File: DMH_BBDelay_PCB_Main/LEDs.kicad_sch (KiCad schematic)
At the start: 7 parts, among them SW2 SW_DPDT_x2

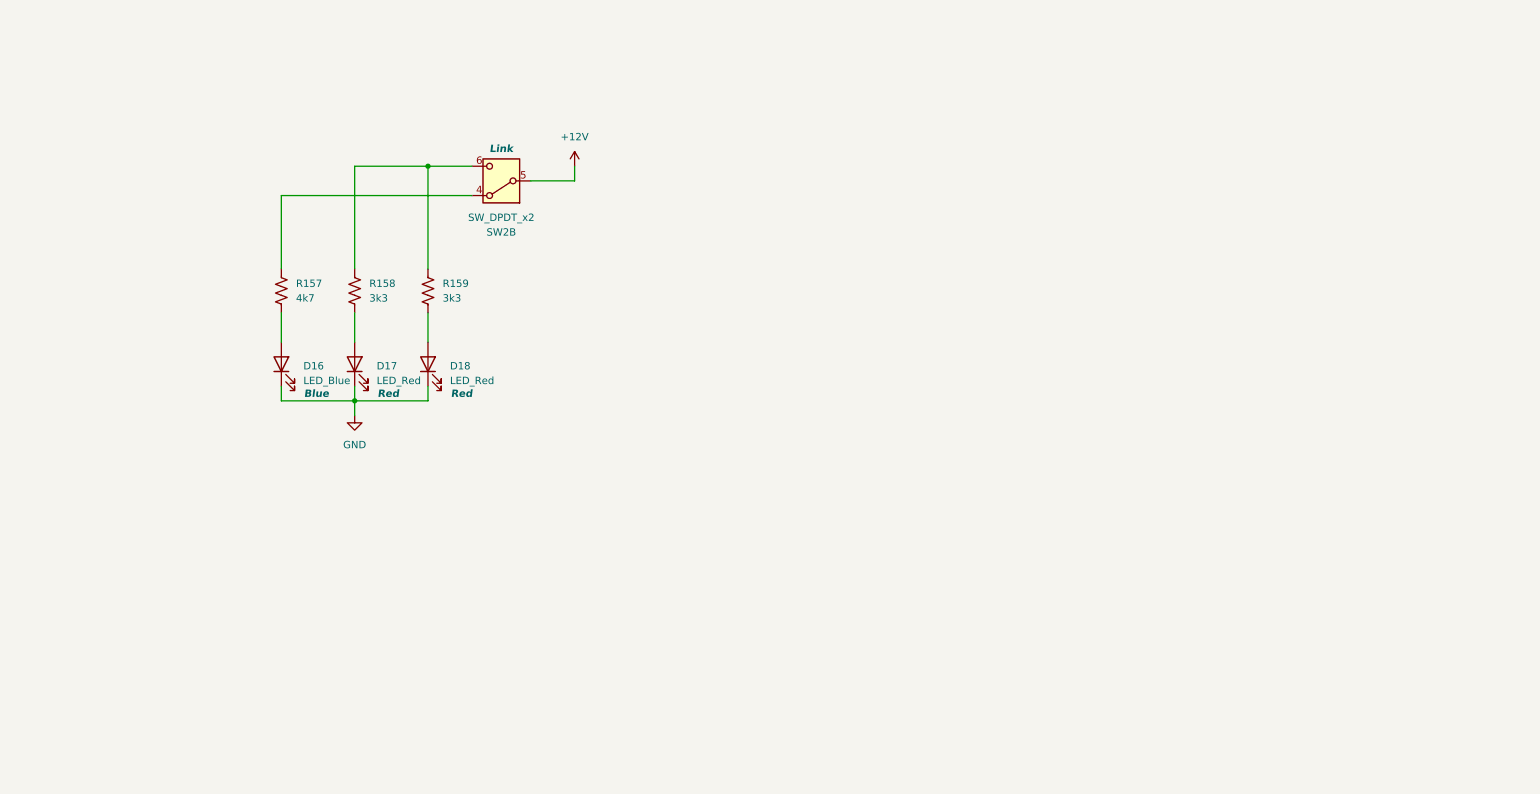
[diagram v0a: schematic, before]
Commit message: Added clock dividers for LEDs
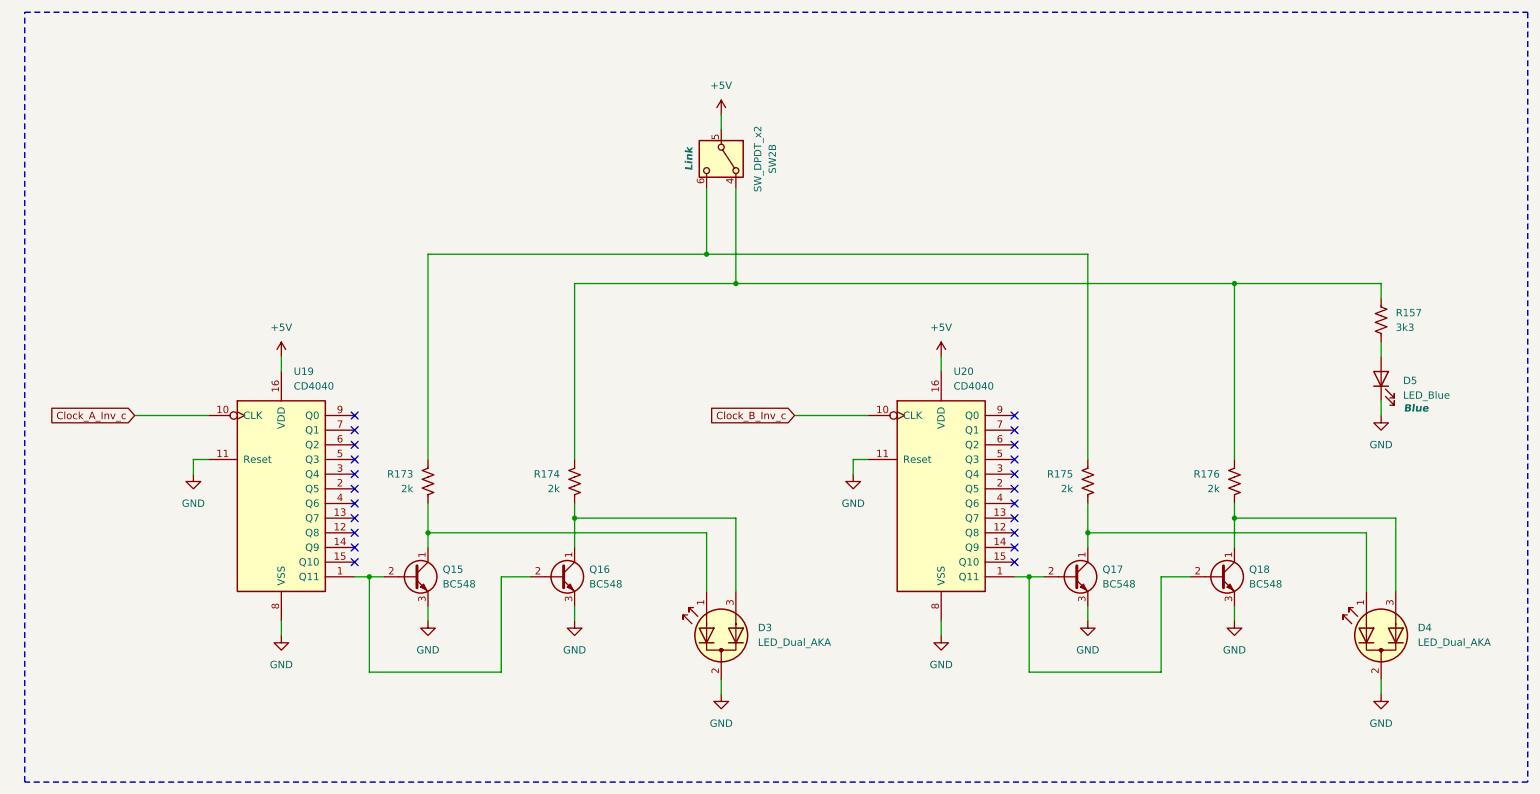
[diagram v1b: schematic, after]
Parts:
- removed D16: LED_Blue, LED_THT:LED_D3.0mm, symbol Device:LED
- removed D17, D18: LED_Red, LED_THT:LED_D3.0mm, symbol Device:LED
- removed R158, R159: 3k3, Resistor_THT:R_Axial_DIN0207_L6.3mm_D2.5mm_P7.62mm_Horizontal, symbol Device:R_US
- added D3, D4: LED_Dual_AKA, SynthStuff:LED_D3.0mm-2color, symbol Device:LED_Dual_AKA
- added D5: LED_Blue, LED_THT:LED_D3.0mm, symbol Device:LED
- added Q15, Q16, Q17, Q18: BC548, Package_TO_SOT_THT:TO-92L_Inline_Wide, symbol Transistor_BJT:BC548
- added R173, R174, R175, R176: 2k, Resistor_THT:R_Axial_DIN0207_L6.3mm_D2.5mm_P7.62mm_Horizontal, symbol Device:R_US
- added U19, U20: CD4040, Package_DIP:DIP-16_W7.62mm_Socket, symbol 4xxx:4040
- R157: value 4k7 -> 3k3
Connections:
- net GND: now also D3.2 (K), D4.2 (K), D5.1 (K), Q15.3 (E), Q16.3 (E), Q17.3 (E), Q18.3 (E), U19.11 (Reset), U19.8 (VSS), U20.11 (Reset), U20.8 (VSS)
- net at R157.2: now also D5.2 (A)
- net at SW2.6 (C): now also R173.2, R175.2
- net at R157.1, SW2.4 (A): now also R174.2, R176.2
- net +12V renamed +5V
- net +5V: now also U19.16 (VDD), U20.16 (VDD)
- new net: D3.1 (A1), Q15.1 (C), R173.1
- new net: Q15.2 (B), Q16.2 (B), U19.1 (Q11)
- new net: D3.3 (A2), Q16.1 (C), R174.1
- new net: D4.3 (A2), Q18.1 (C), R176.1
- new net: D4.1 (A1), Q17.1 (C), R175.1
- new net: Q17.2 (B), Q18.2 (B), U20.1 (Q11)
- new net Clock_A_Inv_c: U19.10 (CLK)
- new net Clock_B_Inv_c: U20.10 (CLK)
- no-connect marks 0 -> 22

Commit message: Connected blue LED to Ping Pong switch
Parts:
- removed D5: LED_Blue, LED_THT:LED_D3.0mm, symbol Device:LED
- removed R157: 3k3, Resistor_THT:R_Axial_DIN0207_L6.3mm_D2.5mm_P7.62mm_Horizontal, symbol Device:R_US

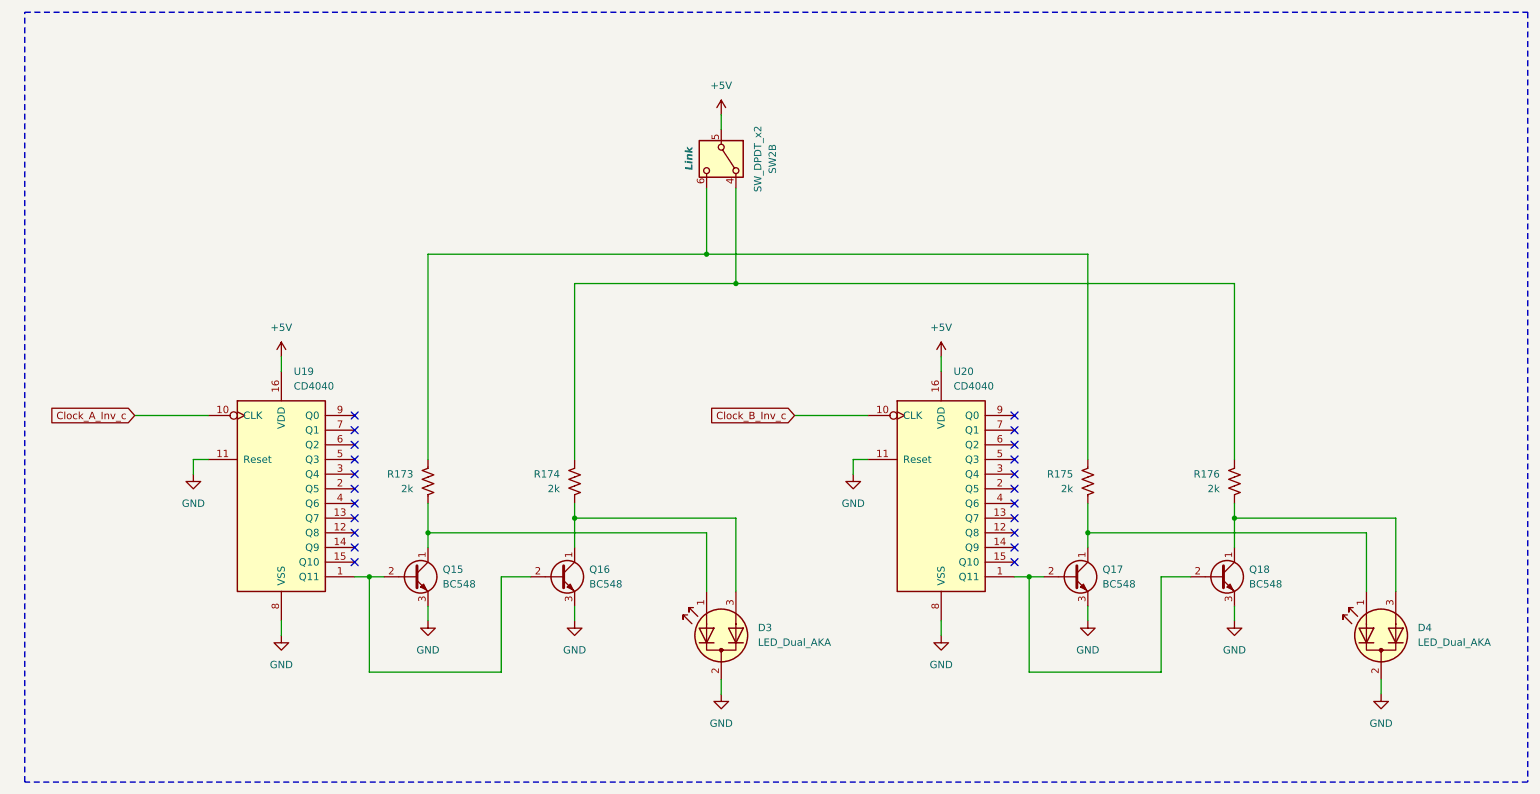
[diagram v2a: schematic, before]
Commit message: Improved LEDs section
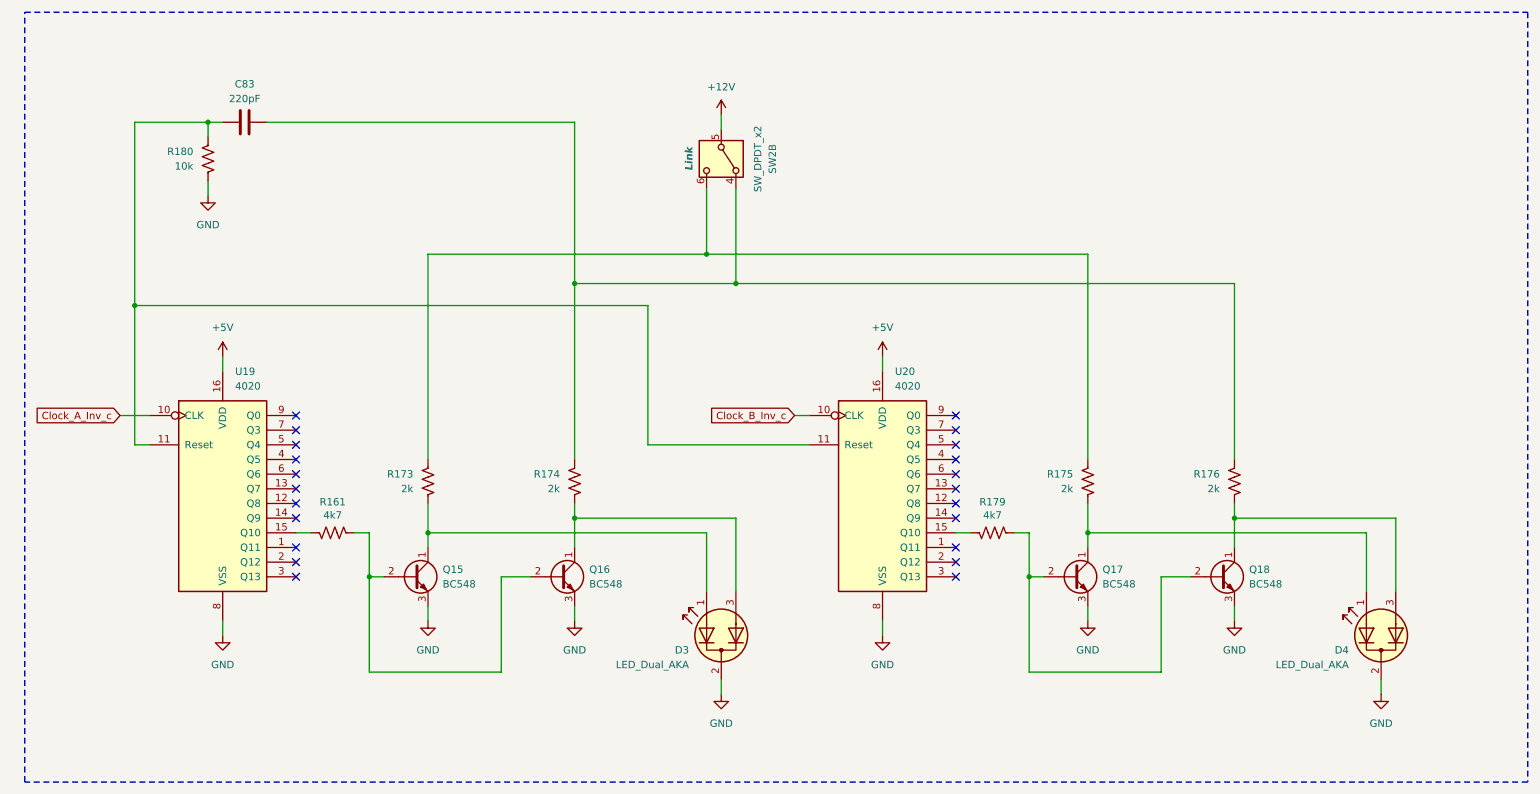
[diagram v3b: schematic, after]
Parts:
- added C83: 220pF, Capacitor_THT:C_Disc_D3.0mm_W2.0mm_P2.50mm, symbol Device:C
- added R161, R179: 4k7, Resistor_THT:R_Axial_DIN0207_L6.3mm_D2.5mm_P7.62mm_Horizontal, symbol Device:R_US
- added R180: 10k, Resistor_THT:R_Axial_DIN0207_L6.3mm_D2.5mm_P7.62mm_Horizontal, symbol Device:R_US
- U19, U20: value CD4040 -> 4020; symbol 4xxx:4040 -> 4xxx:4020
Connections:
- net +5V: no longer SW2.5 (B)
- net GND: now also R180.1; no longer U19.11 (Reset), U20.11 (Reset)
- net at Q15.2 (B), Q16.2 (B): now also R161.2; no longer U19.1 (Q11)
- net at R174.2, R176.2, SW2.4 (A): now also C83.2
- net at U19.15 (Q10): now also R161.1
- net at Q17.2 (B), Q18.2 (B): now also R179.2; no longer U20.1 (Q11)
- net at U20.15 (Q10): now also R179.1
- new net: C83.1, R180.2, U19.11 (Reset), U20.11 (Reset)
- new net +12V: SW2.5 (B)
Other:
- moved on the sheet: U19, U20

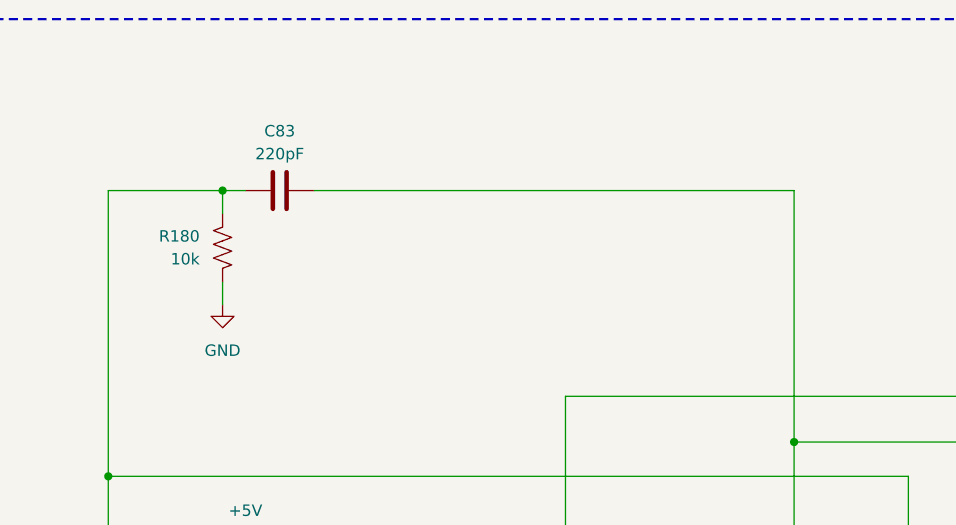
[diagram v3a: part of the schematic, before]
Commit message: Improved safety of LEDs counter reset circuit
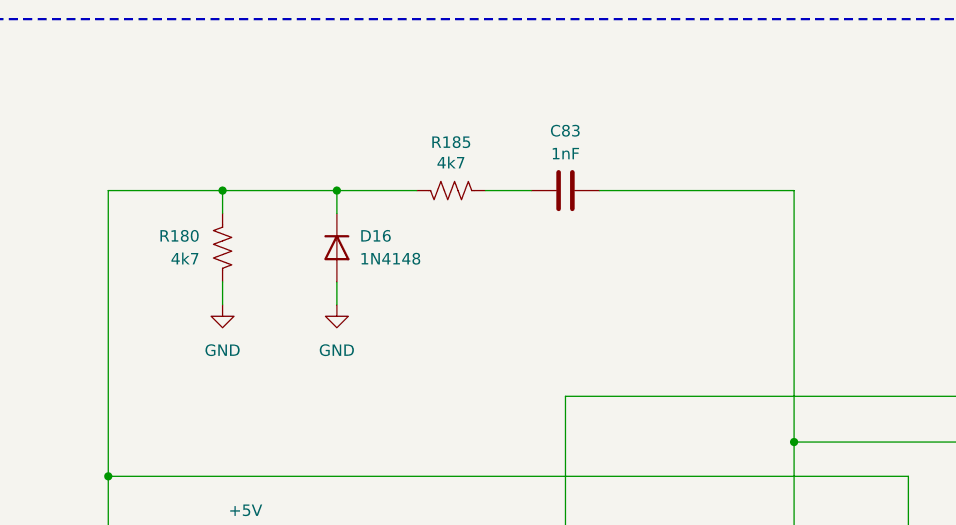
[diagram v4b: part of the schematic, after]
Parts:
- added D16: 1N4148, Diode_THT:D_DO-35_SOD27_P7.62mm_Horizontal, symbol Diode:1N4148
- added R185: 4k7, Resistor_THT:R_Axial_DIN0207_L6.3mm_D2.5mm_P7.62mm_Horizontal, symbol Device:R_US
- C83: value 220pF -> 1nF
- R180: value 10k -> 4k7
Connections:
- net GND: now also D16.2 (A)
- net at R180.2, U19.11 (Reset), U20.11 (Reset): now also D16.1 (K), R185.1; no longer C83.1
- new net: C83.1, R185.2
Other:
- moved on the sheet: C83
